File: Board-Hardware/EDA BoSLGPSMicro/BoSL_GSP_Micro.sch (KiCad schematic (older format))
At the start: 58 parts, among them CON1 Micro_SD_Card, CON2 BARREL_JACK, IC1 ATMEGA328-P, IC2 SIM7000, J1 Screw_Terminal_1x06, J2 Screw_Terminal_1x04, J3 Screw_Terminal_1x02, J4 Screw_Terminal_1x08, J5 Screw_Terminal_1x04, J6 RJ45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

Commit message: started layout of micro bosl gps
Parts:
- removed J1: Screw_Terminal_1x06, SIMFootprints:Screw_Terminals_1x6, symbol SIM7000-rescue:Screw_Terminal_1x06-SIM7000-rescue
- removed J2, J5: Screw_Terminal_1x04, SIMFootprints:Screw_Terminals_1x4, symbol SIM7000-rescue:Screw_Terminal_1x04-SIM7000-rescue
- removed J3: Screw_Terminal_1x02, SIMFootprints:Screw_Terminals_1x2, symbol SIM7000-rescue:Screw_Terminal_1x02-SIM7000-rescue
- removed J4: Screw_Terminal_1x08, SIMFootprints:Screw_Terminals_1x8, symbol SIM7000-rescue:Screw_Terminal_1x08-SIM7000-rescue
- removed J6: RJ45, SIMFootprints:RJ_45, symbol SIM7000-rescue:RJ45-SIM7000-rescue
- removed P1: CONN_01X16, Pin_Headers:Pin_Header_Straight_1x16_Pitch2.54mm, symbol SIM7000-rescue:CONN_01X16-SIM7000-rescue
- removed P3: CONN_01X04, Pin_Headers:Pin_Header_Straight_1x04_Pitch2.54mm, symbol SIM7000-rescue:CONN_01X04-SIM7000-rescue
- removed P6: CONN_01X09, Pin_Headers:Pin_Header_Straight_1x09_Pitch2.54mm, symbol SIM7000-rescue:CONN_01X09-SIM7000-rescue
- removed P9: CONN_01X12, Pin_Headers:Pin_Header_Straight_1x12_Pitch2.54mm, symbol SIM7000-rescue:CONN_01X12-SIM7000-rescue
- removed R2, R3: 10 kΩ, Resistors_SMD:R_0805_HandSoldering, symbol Device:R
- removed U2: MS5803, SIMFootprints:MS5803, symbol SIM7000-rescue:MS5803-simcom
- H1, H2: footprint Mounting_Holes:MountingHole_2.2mm_M2 -> Mounting_Holes:MountingHole_3.2mm_M3
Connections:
- no-connect marks 37 -> 35
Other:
- note removed: "Eithernet Sensor Port"
- note removed: "MS5803 On-Board Pressure Sensor"
- moved on the sheet: P2

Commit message: layout progress of gps micro board
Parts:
- removed IC1: ATMEGA328-P, Housings_DIP:DIP-28_W7.62mm_Socket_LongPads, symbol SIM7000-rescue:ATMEGA328-P-SIM7000-rescue
- added U2: ATmega328P-AU, Housings_QFP:LQFP-32_7x7mm_Pitch0.8mm, symbol MCU_Microchip_ATmega:ATmega328P-AU
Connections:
- net A0: now also U2.23 (PC0)
- net A1: now also U2.24 (PC1)
- net A2: now also U2.25 (PC2)
- net A3: now also U2.26 (PC3)
- net AREF: now also U2.20 (AREF)
- net D6: now also U2.10 (PD6)
- net D7: now also U2.11 (PD7)
- net D8: now also U2.12 (PB0)
- net D9: now also U2.13 (PB1)
- net DTR: now also U2.9 (PD5)
- net GND: now also U2.21 (GND), U2.3 (GND), U2.5 (GND)
- net ONOFF_PIN: now also U2.2 (PD4)
- net RX: now also U2.32 (PD2)
- net SCL: now also U2.28 (PC5)
- net SDA: now also U2.27 (PC4)
- net SD_CS: now also U2.14 (PB2)
- net SD_MISO: now also U2.16 (PB4)
- net SD_MOSI: now also U2.15 (PB3)
- net SD_SCLK: now also U2.17 (PB5)
- net TLL_RST: now also U2.29 (~RESET~/PC6)
- net TLL_RX: now also U2.30 (PD0)
- net TLL_TX: now also U2.31 (PD1)
- net TX: now also U2.1 (PD3)
- net V_3.3: now also U2.18 (AVCC), U2.4 (VCC), U2.6 (VCC)
- net at C3.2, Y1.1: now also U2.8 (XTAL2/PB7)
- net at C2.2, Y1.2: now also U2.7 (XTAL1/PB6)
- new net A6: U2.19 (ADC6)
- new net A7: U2.22 (ADC7)
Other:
- moved on the sheet: R1
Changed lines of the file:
@@
 EESchema Schematic File Version 4
+LIBS:BoSL_GSP_Micro-cache
 EELAYER 29 0
 EELAYER END
@@
 NoConn ~ 7050 1500
 $Comp
-L SIM7000-rescue:ATMEGA328-P-SIM7000-rescue IC1
-U 1 1 5CE615FC
-P 2400 5050
-F 0 "IC1" H 1500 4900 50  0000 L BNN
-F 1 "ATMEGA328-P" H 2800 3650 50  0000 L BNN
-F 2 "Housings_DIP:DIP-28_W7.62mm_Socket_LongPads" H 2400 5050 50  0001 C CIN
-F 3 "" H 2400 5050 50  0000 C CNN
-	1    2400 5050
-	1    0    0    -1
-$EndComp
-$Comp
 L power:GND #PWR03
 U 1 1 5CE61B33
-P 1500 6150
-F 0 "#PWR03" H 1500 5900 50  0001 C CNN
-F 1 "GND" H 1500 6000 50  0000 C CNN
-F 2 "" H 1500 6150 50  0000 C CNN
-F 3 "" H 1500 6150 50  0000 C CNN
-	1    1500 6150
-	0    1    1    0
+P 2800 6650
+F 0 "#PWR03" H 2800 6400 50  0001 C CNN
+F 1 "GND" H 2800 6500 50  0000 C CNN
+F 2 "" H 2800 6650 50  0000 C CNN
+F 3 "" H 2800 6650 50  0000 C CNN
+	1    2800 6650
+	0    -1   -1   0
 $EndComp
 $Comp
 L Device:R R1
 U 1 1 5CE61DD3
-P 3900 5400
-F 0 "R1" V 3980 5400 50  0000 C CNN
-F 1 "10 kΩ" V 3800 5400 50  0000 C CNN
-F 2 "Resistors_SMD:R_0805_HandSoldering" V 3830 5400 50  0001 C CNN
-F 3 "" H 3900 5400 50  0000 C CNN
-	1    3900 5400
-	0    1    1    0
-$EndComp
-Text GLabel 3400 5950 2    60   Input ~ 0
+P 3900 5450
+F 0 "R1" V 3980 5450 50  0000 C CNN
+F 1 "10 kΩ" V 3800 5450 50  0000 C CNN
+F 2 "Resistors_SMD:R_0805_HandSoldering" V 3830 5450 50  0001 C CNN
+F 3 "" H 3900 5450 50  0000 C CNN
+	1    3900 5450
+	0    1    1    0
+$EndComp
+Text GLabel 3400 6050 2    60   Input ~ 0
 ONOFF_PIN
-Text GLabel 3700 5400 1    60   Input ~ 0
+Text GLabel 3700 5450 1    60   Input ~ 0
 TLL_RST
-Text GLabel 3400 5550 2    60   Input ~ 0
+Text GLabel 3400 5650 2    60   Input ~ 0
 TLL_RX
-Text GLabel 3400 5650 2    60   Input ~ 0
+Text GLabel 3400 5750 2    60   Input ~ 0
 TLL_TX
 $Comp
@@
 Text GLabel 1750 7050 0    60   Input ~ 0
 TLL_RST
-Text GLabel 3400 4800 2    60   Input ~ 0
+Text GLabel 3400 4850 2    60   Input ~ 0
 A0
-Text GLabel 3400 5200 2    60   Input ~ 0
+Text GLabel 3400 5250 2    60   Input ~ 0
 SDA
-Text GLabel 3400 5300 2    60   Input ~ 0
+Text GLabel 3400 5350 2    60   Input ~ 0
 SCL
-Text GLabel 3400 4900 2    60   Input ~ 0
+Text GLabel 3400 4950 2    60   Input ~ 0
 A1
-Text GLabel 3400 5000 2    60   Input ~ 0
+Text GLabel 3400 5050 2    60   Input ~ 0
 A2
-Text GLabel 3400 5100 2    60   Input ~ 0
+Text GLabel 3400 5150 2    60   Input ~ 0
 A3
 $Comp
@@
 Text GLabel 6550 2250 0    60   Input ~ 0
 DTR
-Text GLabel 3400 6050 2    60   Input ~ 0
+Text GLabel 3400 6150 2    60   Input ~ 0
 DTR
 $Comp
@@
 Text GLabel 3400 4450 2    60   Input ~ 0
 SD_SCLK
-Text GLabel 3400 5750 2    60   Input ~ 0
+Text GLabel 3400 5850 2    60   Input ~ 0
 RX
-Text GLabel 3400 5850 2    60   Input ~ 0
+Text GLabel 3400 5950 2    60   Input ~ 0
 TX
 Text GLabel 3400 4250 2    60   Input ~ 0
@@
 	1    0    0    -1
 $EndComp
-Text GLabel 3400 6250 2    60   Input ~ 0
+Text GLabel 3400 6350 2    60   Input ~ 0
 D7
 Text GLabel 3400 3950 2    60   Input ~ 0
 D8
-Text GLabel 1500 4550 0    60   Input ~ 0
+Text GLabel 2200 3950 0    60   Input ~ 0
 AREF
 $Comp
@@
 	7850 900  7850 1500
 Wire Wire Line
-	1500 6150 1500 6250
-Wire Wire Line
-	1500 4250 1500 3950
-Wire Wire Line
-	4150 5400 4050 5400
+	4150 5450 4050 5450
 Wire Wire Line
 	3400 4550 4050 4550
@@
 	0    1    1    0
 $EndComp
-Text GLabel 1500 3950 0    60   Input ~ 0
+Text GLabel 2800 3550 1    60   Input ~ 0
 V_3.3
 NoConn ~ 6550 3550
-Text GLabel 3400 6150 2    60   Input ~ 0
+Text GLabel 3400 6250 2    60   Input ~ 0
 D6
 Text GLabel 2650 7250 0    60   Input ~ 0
@@
 	14350 2400 14450 2400
 Wire Wire Line
-	3400 5400 3750 5400
+	3400 5450 3750 5450
 Wire Wire Line
 	8550 5000 9050 5000
@@
 Text Notes 9750 3800 0    60   ~ 0
 Mounting Holes\n
-Text GLabel 4150 5400 2    60   Input ~ 0
+Text GLabel 4150 5450 2    60   Input ~ 0
 V_3.3
 $Comp
@@
 	0    1    1    0
 $EndComp
+$Comp
+L MCU_Microchip_ATmega:ATmega328P-AU U2
+U 1 1 5DE0CED2
+P 2800 5150
+F 0 "U2" H 2800 3563 50  0000 C CNN
+F 1 "ATmega328P-AU" H 2800 3474 50  0000 C CNN
+F 2 "Housings_QFP:LQFP-32_7x7mm_Pitch0.8mm" H 2800 5150 50  0001 C CIN
+F 3 "http://ww1.microchip.com/downloads/en/DeviceDoc/ATmega328_P%20AVR%20MCU%20with%20picoPower%20Technology%20Data%20Sheet%2040001984A.pdf" H 2800 5150 50  0001 C CNN
+	1    2800 5150
+	1    0    0    -1
+$EndComp
+Wire Wire Line
+	2900 3650 2900 3550
+Wire Wire Line
+	2900 3550 2800 3550
+Wire Wire Line
+	2800 3650 2800 3550
+Text GLabel 2200 4150 0    60   Input ~ 0
+A6
+Text GLabel 2200 4250 0    60   Input ~ 0
+A7
 $EndSCHEMATC

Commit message: finished parts list for BoSL GPS Micro
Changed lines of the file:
@@
 encoding utf-8
 Sheet 1 1
-Title "Monash BoSL G Board"
-Date "2019-11-01"
-Rev "0.3 G"
+Title "Monash BoSL GPS Micro Board"
+Date "2019-11-29"
+Rev "0.3 Gμ"
 Comp ""
 Comment1 ""
@@
 P 2800 5150
 F 0 "U2" H 2800 3563 50  0000 C CNN
-F 1 "ATmega328P-AU" H 2800 3474 50  0000 C CNN
+F 1 "ATmega328P-AU" H 3500 3700 50  0000 C CNN
 F 2 "Housings_QFP:LQFP-32_7x7mm_Pitch0.8mm" H 2800 5150 50  0001 C CIN
 F 3 "http://ww1.microchip.com/downloads/en/DeviceDoc/ATmega328_P%20AVR%20MCU%20with%20picoPower%20Technology%20Data%20Sheet%2040001984A.pdf" H 2800 5150 50  0001 C CNN

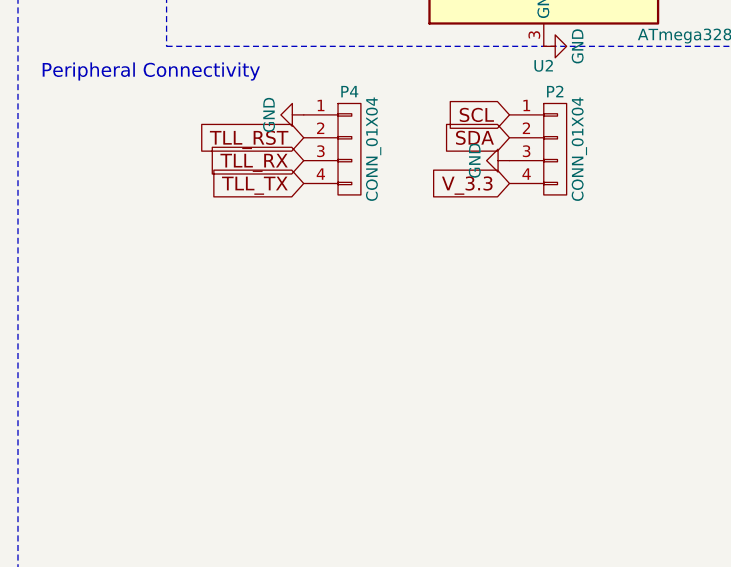
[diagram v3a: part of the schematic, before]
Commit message: added spi header to bosl GPS micro for bootloading
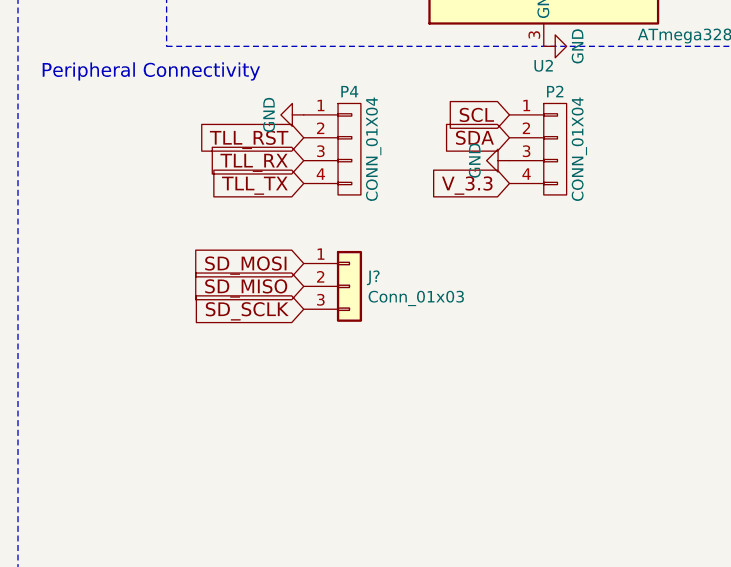
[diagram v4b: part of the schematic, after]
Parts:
- added J?: Conn_01x03, symbol Connector_Generic:Conn_01x03
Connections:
- net SD_MISO: now also J?.2 (Pin_2)
- net SD_MOSI: now also J?.1 (Pin_1)
- net SD_SCLK: now also J?.3 (Pin_3)
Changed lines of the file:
@@
 Text GLabel 2200 4250 0    60   Input ~ 0
 A7
+$Comp
+L Connector_Generic:Conn_01x03 J?
+U 1 1 5DE48010
+P 1950 7700
+F 0 "J?" H 2030 7742 50  0000 L CNN
+F 1 "Conn_01x03" H 2030 7653 50  0000 L CNN
+F 2 "" H 1950 7700 50  0001 C CNN
+F 3 "~" H 1950 7700 50  0001 C CNN
+	1    1950 7700
+	1    0    0    -1
+$EndComp
+Text GLabel 1750 7600 0    60   Input ~ 0
+SD_MOSI
+Text GLabel 1750 7700 0    60   Input ~ 0
+SD_MISO
+Text GLabel 1750 7800 0    60   Input ~ 0
+SD_SCLK
 $EndSCHEMATC
